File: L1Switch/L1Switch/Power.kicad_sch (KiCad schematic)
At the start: 70 parts, among them J3 Barrel_Jack, M1 Fan, M2 Fan, U3 TPS548A20RVE, U4 TPS565208, U5 TPS565208, U6 TPS565208

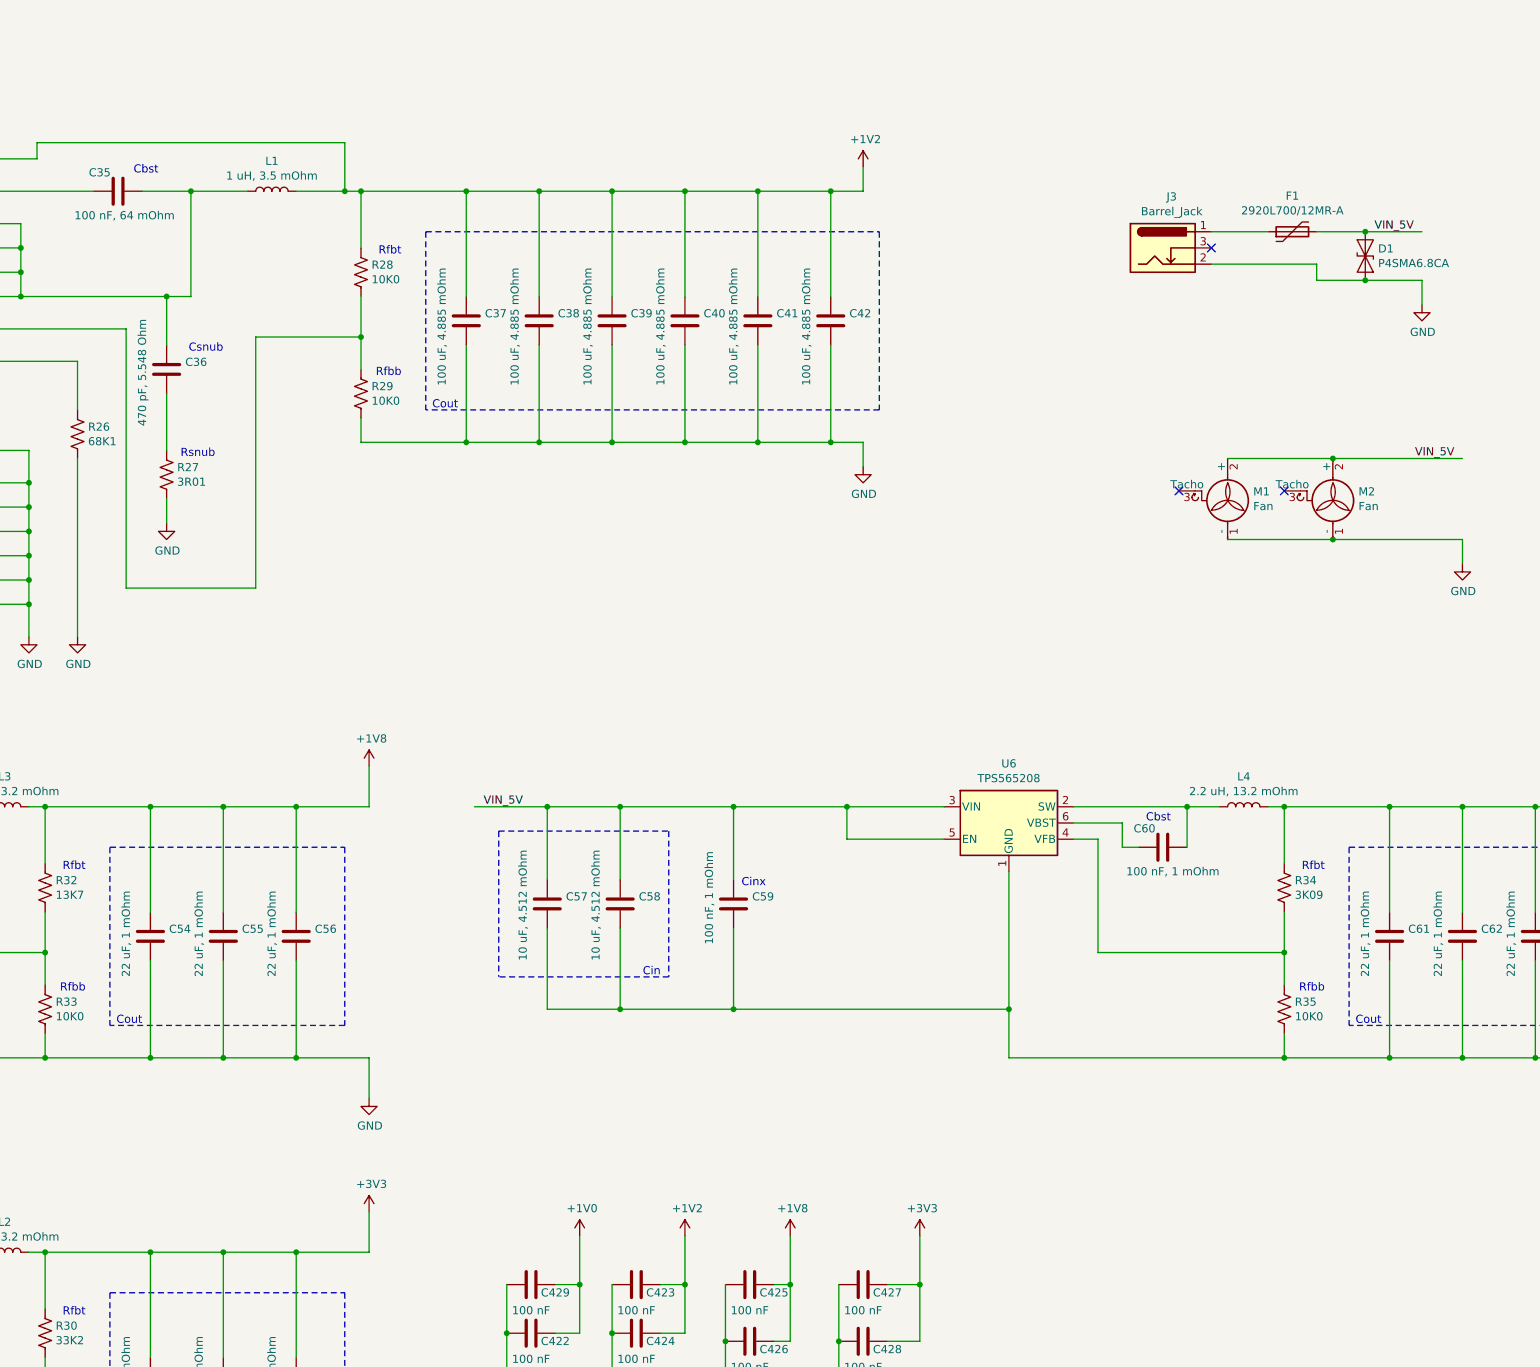
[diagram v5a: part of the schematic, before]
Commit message: Add PWR_FLAG to clean up ERC errors about undriven nets. Change R269 from 100K0 to 10K0.
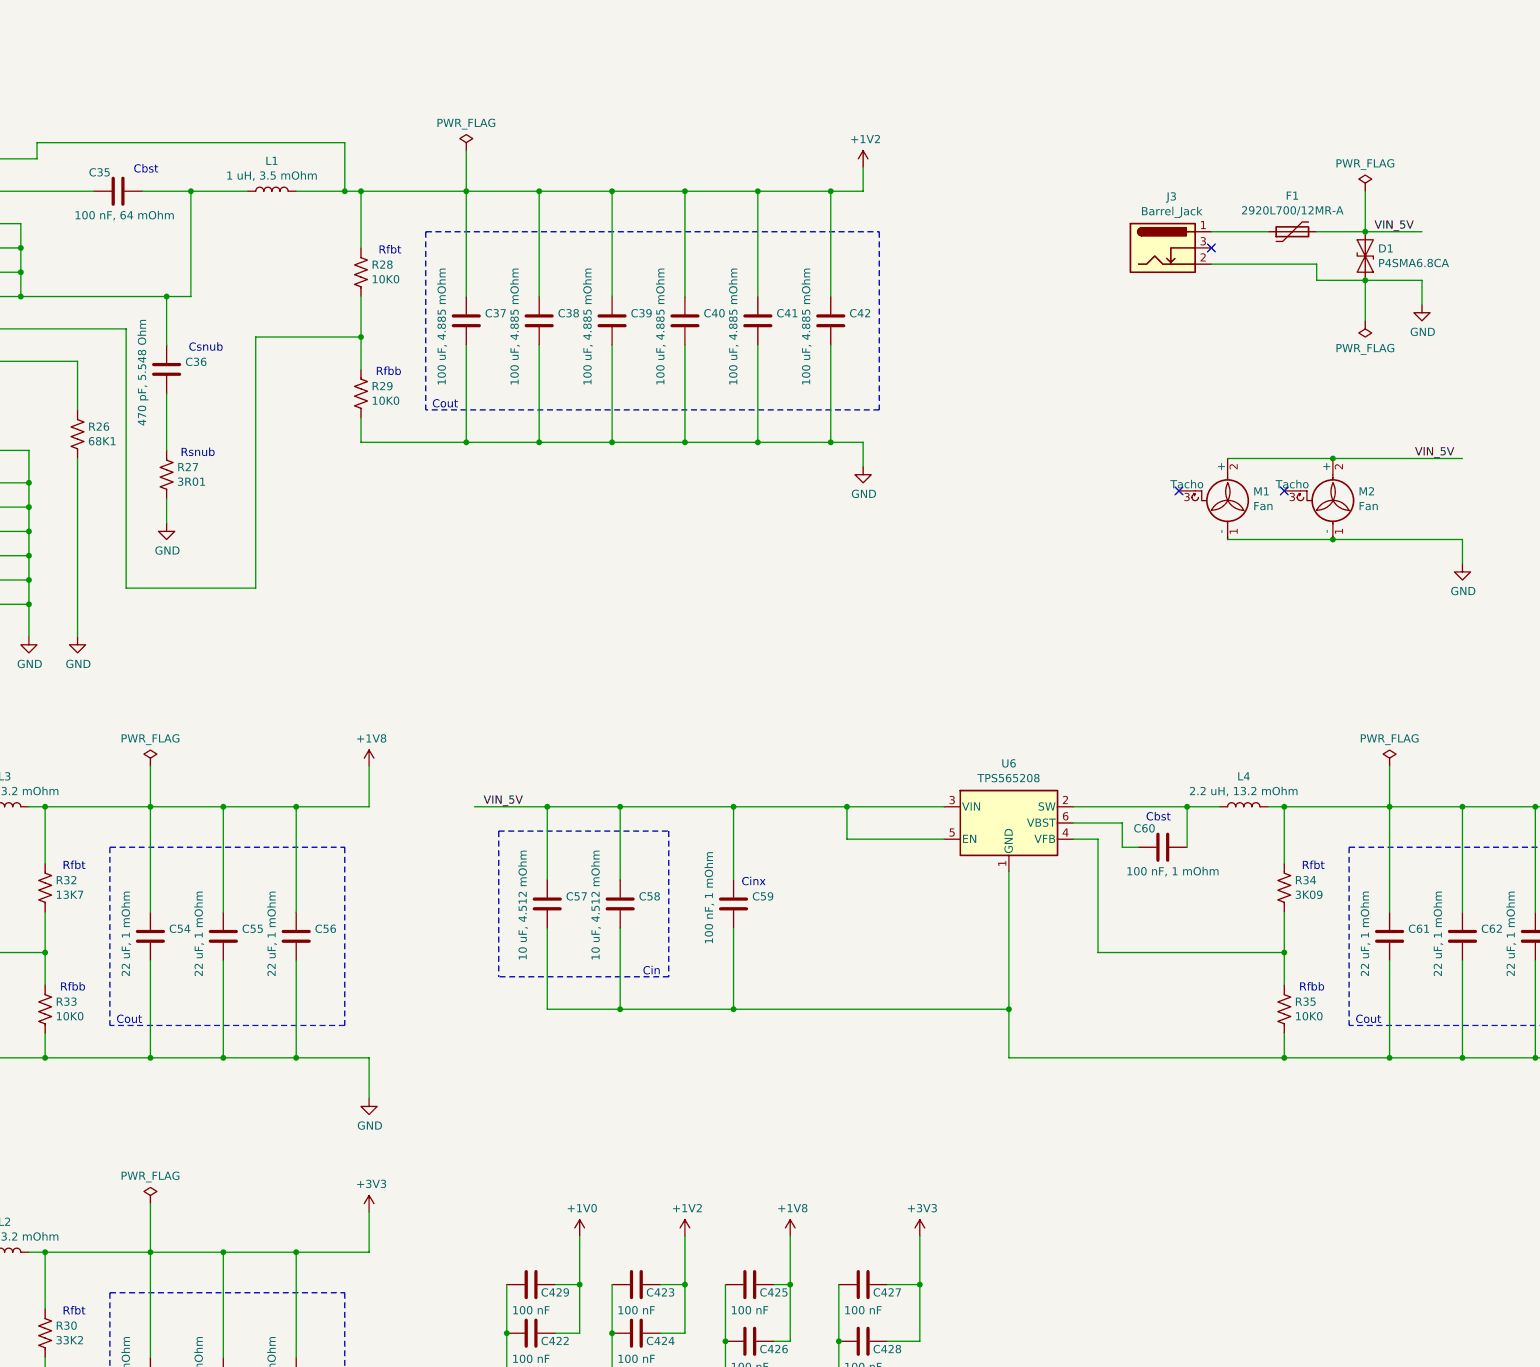
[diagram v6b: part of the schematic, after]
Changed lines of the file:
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@@
-(kicad_sch (version 20200608) (host eeschema "5.99.0-unknown-1973153~101~ubuntu20.04.1")
-  (page 1 12)
+(kicad_sch (version 20200608) (host eeschema "(5.99.0-1946-g60915fbc7)")
+  (page 12 12)
   (paper "B")
   (junction (at 26.67 80.01))
@@
   (junction (at 396.24 143.51))
   (junction (at 396.24 182.88))
+  (no_connect (at 356.87 93.98))
   (no_connect (at 345.44 55.88))
-  (no_connect (at 356.87 93.98))
   (no_connect (at 340.36 93.98))
   (wire (pts (xy 20.32 48.26) (xy 29.21 48.26))
@@
     (stroke (width 0) (type solid) (color 0 0 0 0))
   )
+  (wire (pts (xy 179.07 137.16) (xy 179.07 143.51))
+    (stroke (width 0) (type solid) (color 0 0 0 0))
+  )
   (wire (pts (xy 179.07 143.51) (xy 179.07 160.02))
     (stroke (width 0) (type solid) (color 0 0 0 0))
@@
     (stroke (width 0) (type solid) (color 0 0 0 0))
   )
+  (wire (pts (xy 179.07 205.74) (xy 179.07 213.36))
+    (stroke (width 0) (type solid) (color 0 0 0 0))
+  )
   (wire (pts (xy 179.07 213.36) (xy 179.07 229.87))
     (stroke (width 0) (type solid) (color 0 0 0 0))
@@
     (stroke (width 0) (type solid) (color 0 0 0 0))
   )
+  (wire (pts (xy 228.6 40.64) (xy 228.6 46.99))
+    (stroke (width 0) (type solid) (color 0 0 0 0))
+  )
   (wire (pts (xy 228.6 46.99) (xy 228.6 63.5))
     (stroke (width 0) (type solid) (color 0 0 0 0))
@@
     (stroke (width 0) (type solid) (color 0 0 0 0))
   )
+  (wire (pts (xy 369.57 46.99) (xy 369.57 53.34))
+    (stroke (width 0) (type solid) (color 0 0 0 0))
+  )
   (wire (pts (xy 369.57 53.34) (xy 378.46 53.34))
     (stroke (width 0) (type solid) (color 0 0 0 0))
@@
     (stroke (width 0) (type solid) (color 0 0 0 0))
   )
+  (wire (pts (xy 369.57 60.96) (xy 369.57 67.31))
+    (stroke (width 0) (type solid) (color 0 0 0 0))
+  )
   (wire (pts (xy 369.57 60.96) (xy 378.46 60.96))
+    (stroke (width 0) (type solid) (color 0 0 0 0))
+  )
+  (wire (pts (xy 373.38 137.16) (xy 373.38 143.51))
     (stroke (width 0) (type solid) (color 0 0 0 0))
   )
@@
     (effects (font (size 1.27 1.27)) (justify right bottom))
   )
+  (symbol (lib_id "power:PWR_FLAG") (at 179.07 137.16 0) (unit 1)
+    (in_bom yes) (on_board yes)
+    (property "Reference" "#FLG0102" (id 0) (at 179.07 135.255 0)
+      (effects (font (size 1.27 1.27)) hide)
+    )
+    (property "Value" "PWR_FLAG" (id 1) (at 179.07 132.8356 0))
+    (property "Footprint" "" (id 2) (at 179.07 137.16 0)
+      (effects (font (size 1.27 1.27)) hide)
+    )
+    (property "Datasheet" "~" (id 3) (at 179.07 137.16 0)
+      (effects (font (size 1.27 1.27)) hide)
+    )
+  )
+  (symbol (lib_id "power:PWR_FLAG") (at 179.07 205.74 0) (unit 1)
+    (in_bom yes) (on_board yes)
+    (property "Reference" "#FLG0104" (id 0) (at 179.07 203.835 0)
+      (effects (font (size 1.27 1.27)) hide)
+    )
+    (property "Value" "PWR_FLAG" (id 1) (at 179.07 201.4156 0))
+    (property "Footprint" "" (id 2) (at 179.07 205.74 0)
+      (effects (font (size 1.27 1.27)) hide)
+    )
+    (property "Datasheet" "~" (id 3) (at 179.07 205.74 0)
+      (effects (font (size 1.27 1.27)) hide)
+    )
+  )
+  (symbol (lib_id "power:PWR_FLAG") (at 228.6 40.64 0) (unit 1)
+    (in_bom yes) (on_board yes)
+    (property "Reference" "#FLG0103" (id 0) (at 228.6 38.735 0)
+      (effects (font (size 1.27 1.27)) hide)
+    )
+    (property "Value" "PWR_FLAG" (id 1) (at 228.6 36.3156 0))
+    (property "Footprint" "" (id 2) (at 228.6 40.64 0)
+      (effects (font (size 1.27 1.27)) hide)
+    )
+    (property "Datasheet" "~" (id 3) (at 228.6 40.64 0)
+      (effects (font (size 1.27 1.27)) hide)
+    )
+  )
+  (symbol (lib_id "power:PWR_FLAG") (at 369.57 46.99 0) (unit 1)
+    (in_bom yes) (on_board yes)
+    (property "Reference" "#FLG0101" (id 0) (at 369.57 45.085 0)
+      (effects (font (size 1.27 1.27)) hide)
+    )
+    (property "Value" "PWR_FLAG" (id 1) (at 369.57 42.6656 0))
+    (property "Footprint" "" (id 2) (at 369.57 46.99 0)
+      (effects (font (size 1.27 1.27)) hide)
+    )
+    (property "Datasheet" "~" (id 3) (at 369.57 46.99 0)
+      (effects (font (size 1.27 1.27)) hide)
+    )
+  )
+  (symbol (lib_id "power:PWR_FLAG") (at 369.57 67.31 180) (unit 1)
+    (in_bom yes) (on_board yes)
+    (property "Reference" "#FLG0114" (id 0) (at 369.57 69.215 0)
+      (effects (font (size 1.27 1.27)) hide)
+    )
+    (property "Value" "PWR_FLAG" (id 1) (at 369.57 71.6344 0))
+    (property "Footprint" "" (id 2) (at 369.57 67.31 0)
+      (effects (font (size 1.27 1.27)) hide)
+    )
+    (property "Datasheet" "~" (id 3) (at 369.57 67.31 0)
+      (effects (font (size 1.27 1.27)) hide)
+    )
+  )
+  (symbol (lib_id "power:PWR_FLAG") (at 373.38 137.16 0) (unit 1)
+    (in_bom yes) (on_board yes)
+    (property "Reference" "#FLG0105" (id 0) (at 373.38 135.255 0)
+      (effects (font (size 1.27 1.27)) hide)
+    )
+    (property "Value" "PWR_FLAG" (id 1) (at 373.38 132.8356 0))
+    (property "Footprint" "" (id 2) (at 373.38 137.16 0)
+      (effects (font (size 1.27 1.27)) hide)
+    )
+    (property "Datasheet" "~" (id 3) (at 373.38 137.16 0)
+      (effects (font (size 1.27 1.27)) hide)
+    )
+  )
   (symbol (lib_id "power:+1V8") (at 95.25 223.52 0) (unit 1)
